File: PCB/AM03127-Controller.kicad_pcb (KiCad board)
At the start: 2 copper layers, 23 x 76 mm, 17 parts, among them U1 AP63205WU, U2 XIAO-ESP32-C3-DIP, U3 MAX3232

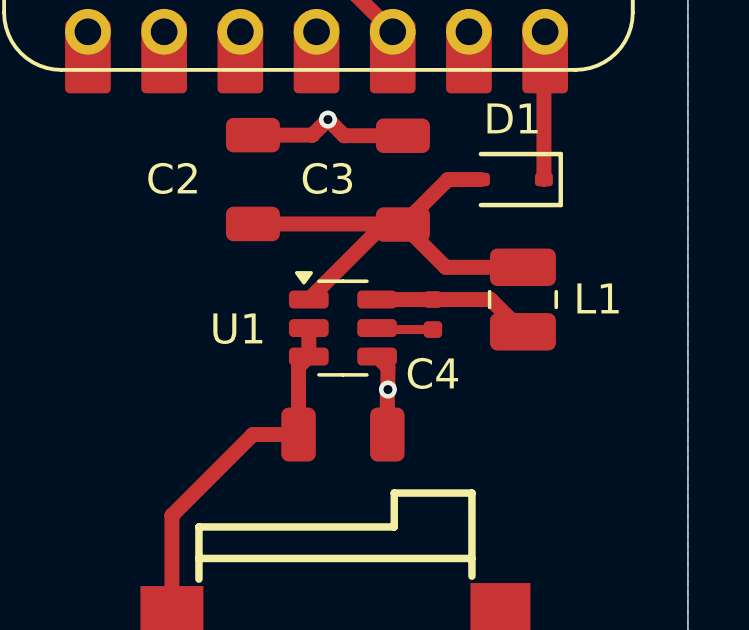
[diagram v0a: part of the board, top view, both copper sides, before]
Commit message: Fix swaped pin for voltage regulator in PCB
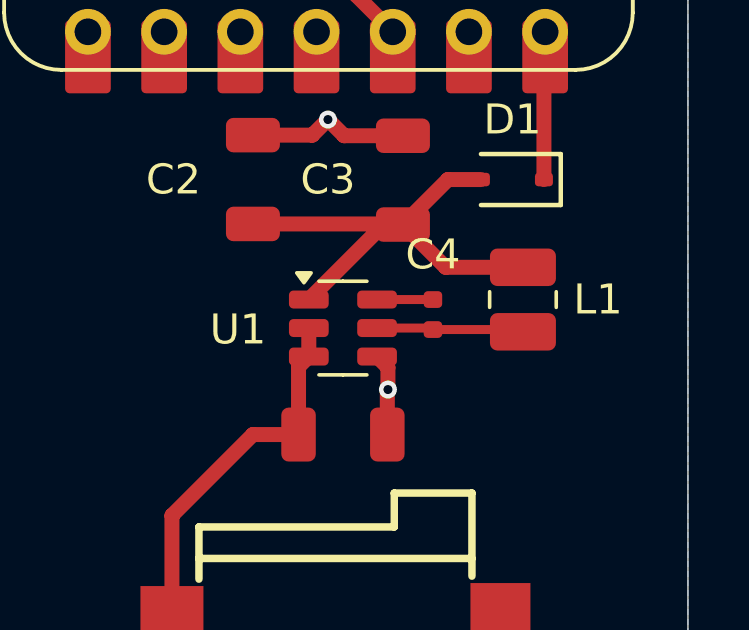
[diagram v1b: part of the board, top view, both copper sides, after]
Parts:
- turned C4 to -90 degrees
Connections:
- C4 pad 1: Net-(U1-SW) -> Net-(U1-BST)
- U1 pad 5: Net-(U1-SW) -> /BuckOut
- U1 pad 6: /BuckOut -> Net-(U1-BST)
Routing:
- net Net-(U1-SW): track 1.88 -> 0.00 mm
- net Net-(U1-BST): track 0.00 -> 1.86 mm
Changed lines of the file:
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@@
 	(net 9 "+3.3V")
 	(net 10 "/RS232 TX")
-	(net 11 "Net-(U1-SW)")
+	(net 11 "Net-(U1-BST)")
 	(net 12 "unconnected-(U2-GPIO4{slash}A2{slash}D2-Pad3)")
 	(net 13 "unconnected-(U2-GPIO7{slash}D5{slash}SCL-Pad6)")
@@
 	(footprint "PCM_JLCPCB:C_0402"
 		(layer "F.Cu")
-		(at 138.5 122.5 90)
+		(at 138.5 122.5 -90)
 		(descr "Capacitor SMD 0402 (1005 Metric), square (rectangular) end terminal, IPC_7351 nominal, (Body size source: IPC-SM-782 page 76, https://www.pcb-3d.com/wordpress/wp-content/uploads/ipc-sm-782a_amendment_1_and_2.pdf), generated with kicad-footprint-generator")
 		(tags "capacitor")
 		(property "Reference" "C4"
-			(at -2 0 180)
+			(at -2 0 0)
 			(layer "F.SilkS")
 			(effects
@@
 		)
 		(property "Datasheet" "https://www.lcsc.com/datasheet/lcsc_datasheet_2304140030_Samsung-Electro-Mechanics-CL05B104KO5NNNC_C1525.pdf"
-			(at 0 0 90)
+			(at 0 0 270)
 			(unlocked yes)
 			(layer "F.Fab")
@@
 		)
 		(property "Description" "16V 100nF X7R ±10% 0402 Multilayer Ceramic Capacitors MLCC - SMD/SMT ROHS"
-			(at 0 0 90)
+			(at 0 0 270)
 			(unlocked yes)
 			(layer "F.Fab")
@@
 		)
 		(property "LCSC" "C1525"
-			(at 0 0 90)
+			(at 0 0 270)
 			(unlocked yes)
 			(layer "F.Fab")
@@
 		)
 		(property "Stock" "20208285"
-			(at 0 0 90)
+			(at 0 0 270)
 			(unlocked yes)
 			(layer "F.Fab")
@@
 		)
 		(property "Price" "0.004USD"
-			(at 0 0 90)
+			(at 0 0 270)
 			(unlocked yes)
 			(layer "F.Fab")
@@
 		)
 		(property "Process" "SMT"
-			(at 0 0 90)
+			(at 0 0 270)
 			(unlocked yes)
 			(layer "F.Fab")
@@
 		)
 		(property "Minimum Qty" "20"
-			(at 0 0 90)
+			(at 0 0 270)
 			(unlocked yes)
 			(layer "F.Fab")
@@
 		)
 		(property "Attrition Qty" "10"
-			(at 0 0 90)
+			(at 0 0 270)
 			(unlocked yes)
 			(layer "F.Fab")
@@
 		)
 		(property "Class" "Basic Component"
-			(at 0 0 90)
+			(at 0 0 270)
 			(unlocked yes)
 			(layer "F.Fab")
@@
 		)
 		(property "Category" "Capacitors,Multilayer Ceramic Capacitors MLCC - SMD/SMT"
-			(at 0 0 90)
+			(at 0 0 270)
 			(unlocked yes)
 			(layer "F.Fab")
@@
 		)
 		(property "Manufacturer" "Samsung Electro-Mechanics"
-			(at 0 0 90)
+			(at 0 0 270)
 			(unlocked yes)
 			(layer "F.Fab")
@@
 		)
 		(property "Part" "CL05B104KO5NNNC"
-			(at 0 0 90)
+			(at 0 0 270)
 			(unlocked yes)
 			(layer "F.Fab")
@@
 		)
 		(property "Voltage Rated" "16V"
-			(at 0 0 90)
+			(at 0 0 270)
 			(unlocked yes)
 			(layer "F.Fab")
@@
 		)
 		(property "Tolerance" "±10%"
-			(at 0 0 90)
+			(at 0 0 270)
 			(unlocked yes)
 			(layer "F.Fab")
@@
 		)
 		(property "Capacitance" "100nF"
-			(at 0 0 90)
+			(at 0 0 270)
 			(unlocked yes)
 			(layer "F.Fab")
@@
 		)
 		(property "Temperature Coefficient" "X7R"
-			(at 0 0 90)
+			(at 0 0 270)
 			(unlocked yes)
 			(layer "F.Fab")
@@
 		(attr smd)
 		(fp_line
-			(start 0.9 -0.4)
-			(end 0.9 0.4)
+			(start 0.9 0.4)
+			(end -0.9 0.4)
 			(stroke
 				(width 0.05)
@@
 		(fp_line
 			(start -0.9 -0.4)
-			(end 0.9 -0.4)
+			(end -0.9 0.4)
 			(stroke
 				(width 0.05)
@@
 		(fp_line
 			(start -0.9 -0.4)
-			(end -0.9 0.4)
+			(end 0.9 -0.4)
 			(stroke
 				(width 0.05)
@@
 		)
 		(fp_line
-			(start 0.9 0.4)
-			(end -0.9 0.4)
+			(start 0.9 -0.4)
+			(end 0.9 0.4)
 			(stroke
 				(width 0.05)
@@
 		)
 		(fp_line
-			(start 0.5 -0.25)
-			(end 0.5 0.25)
+			(start -0.5 0.25)
+			(end -0.5 -0.25)
 			(stroke
 				(width 0.1)
@@
 		)
 		(fp_line
-			(start -0.5 -0.25)
-			(end 0.5 -0.25)
+			(start 0.5 0.25)
+			(end -0.5 0.25)
 			(stroke
 				(width 0.1)
@@
 		)
 		(fp_line
-			(start 0.5 0.25)
-			(end -0.5 0.25)
+			(start -0.5 -0.25)
+			(end 0.5 -0.25)
 			(stroke
 				(width 0.1)
@@
 		)
 		(fp_line
-			(start -0.5 0.25)
-			(end -0.5 -0.25)
+			(start 0.5 -0.25)
+			(end 0.5 0.25)
 			(stroke
 				(width 0.1)
@@
 		)
 		(pad "1" smd roundrect
-			(at -0.5 0 90)
+			(at -0.5 0 270)
 			(size 0.56 0.62)
 			(layers "F.Cu" "F.Mask" "F.Paste")
 			(roundrect_rratio 0.25)
-			(net 11 "Net-(U1-SW)")
+			(net 11 "Net-(U1-BST)")
 			(pintype "passive")
 		)
 		(pad "2" smd roundrect
-			(at 0.5 0 90)
+			(at 0.5 0 270)
 			(size 0.56 0.62)
 			(layers "F.Cu" "F.Mask" "F.Paste")
@@
 			(layers "F.Cu" "F.Mask" "F.Paste")
 			(roundrect_rratio 0.25)
-			(net 11 "Net-(U1-SW)")
+			(net 40 "/BuckOut")
 			(pinfunction "SW")
 			(pintype "output")
@@
 			(layers "F.Cu" "F.Mask" "F.Paste")
 			(roundrect_rratio 0.25)
-			(net 40 "/BuckOut")
+			(net 11 "Net-(U1-BST)")
 			(pinfunction "BST")
 			(pintype "passive")
@@
 	)
 	(segment
-		(start 138.5 123)
-		(end 136.6875 123)
-		(width 0.3)
-		(layer "F.Cu")
-		(net 11)
-	)
-	(segment
-		(start 136.6875 123)
-		(end 136.6375 122.95)
+		(start 136.6375 122)
+		(end 138.5 122)
 		(width 0.3)
 		(layer "F.Cu")
@@
 	)
 	(segment
-		(start 136.6375 122)
-		(end 138.5 122)
-		(width 0.5)
+		(start 138.45 122.95)
+		(end 138.5 123)
+		(width 0.3)
 		(layer "F.Cu")
 		(net 40)
 	)
 	(segment
-		(start 141.5 123.075)
-		(end 140.425 122)
-		(width 0.5)
+		(start 141.425 123)
+		(end 141.5 123.075)
+		(width 0.3)
 		(layer "F.Cu")
 		(net 40)
 	)
 	(segment
-		(start 140.425 122)
-		(end 138.5 122)
-		(width 0.5)
+		(start 136.6875 123)
+		(end 136.6375 122.95)
+		(width 0.3)
+		(layer "F.Cu")
+		(net 40)
+	)
+	(segment
+		(start 136.6375 122.95)
+		(end 138.45 122.95)
+		(width 0.3)
+		(layer "F.Cu")
+		(net 40)
+	)
+	(segment
+		(start 138.5 123)
+		(end 141.425 123)
+		(width 0.3)
 		(layer "F.Cu")
 		(net 40)
